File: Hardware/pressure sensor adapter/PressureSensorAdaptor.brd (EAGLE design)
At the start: 34.3 x 26.7 mm, 13 parts, among them IC1 RCV420P

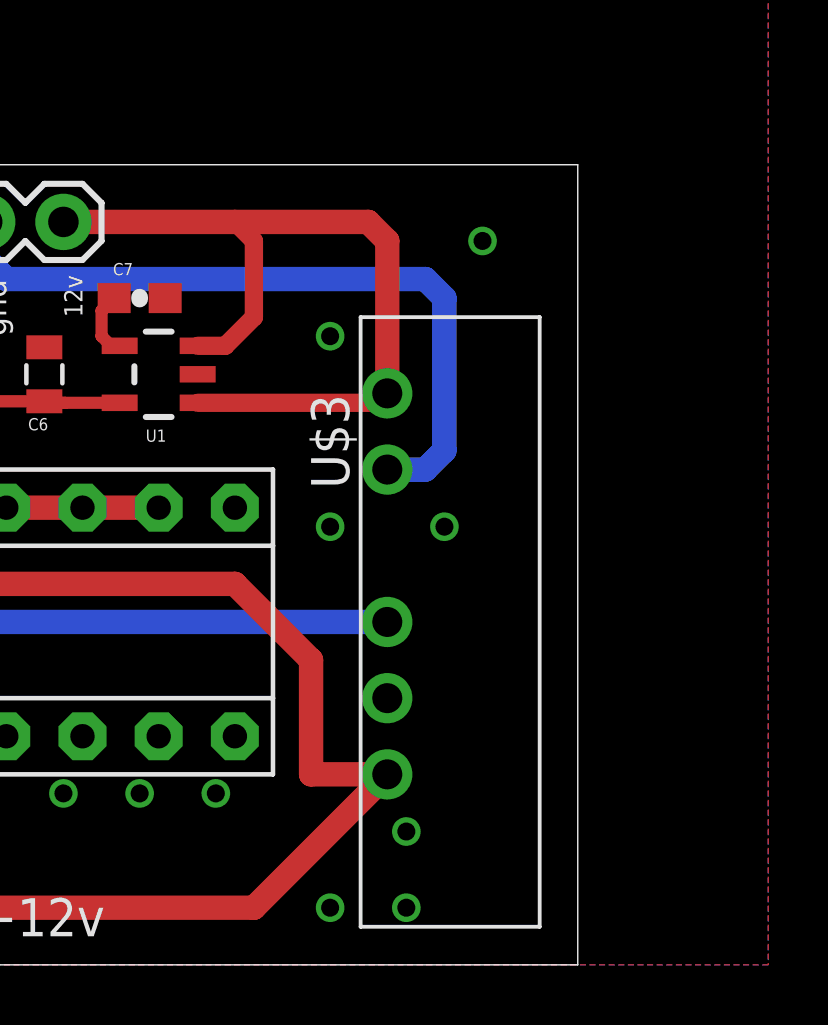
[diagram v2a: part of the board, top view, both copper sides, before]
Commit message: added bulk capacitance on 12v unisolated rail
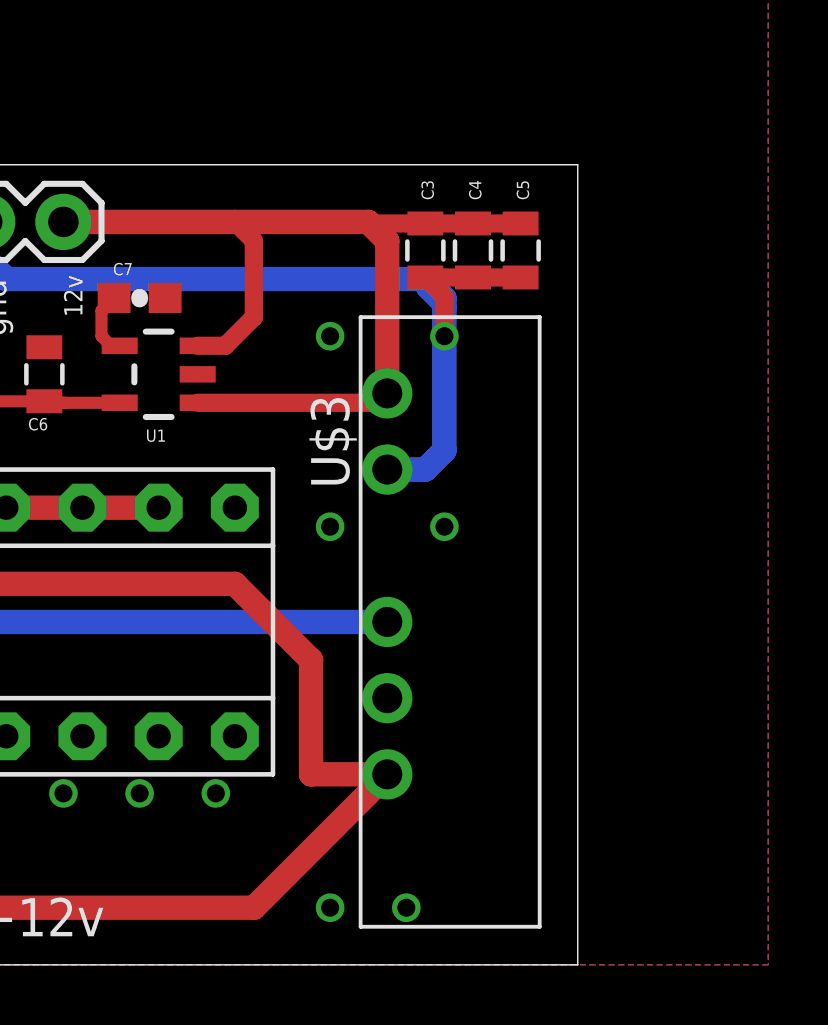
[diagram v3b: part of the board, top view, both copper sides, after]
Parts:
- added C3: 10uF, SparkFun-Capacitors:0805
- added C4: 0.1uf, SparkFun-Capacitors:0805
- added C5: 100pF, SparkFun-Capacitors:0805
- C8: value (none) -> 0.1uf
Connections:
- net 12V: now also C3.1, C4.1, C5.1
- net GND: now also C3.2, C4.2, C5.2
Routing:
- net GND: track 24.3 -> 30.9 mm, vias 0 -> 1
- net 12V: track 28.3 -> 33.4 mm
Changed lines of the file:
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@@
 <attribute name="NAME" x="18.796" y="22.987" size="0.4064" layer="25" font="vector"/>
 </element>
-<element name="C8" library="SparkFun-Capacitors" package="0805" value="" x="3.175" y="19.05" rot="R180"/>
+<element name="C8" library="SparkFun-Capacitors" package="0805" value="0.1uf" x="3.175" y="19.05" rot="R180"/>
 <element name="JP3" library="SparkFun-Connectors" package="1X05" value="" x="6.985" y="24.765" smashed="yes">
 <attribute name="VALUE" x="5.715" y="21.59" size="1.27" layer="27"/>
@@
 </element>
 <element name="U$1" library="RitLaunchInitiative" package="RITLAUNCH_LOGO_SMALLB" value="" x="20.32" y="13.97"/>
+<element name="C3" library="SparkFun-Capacitors" package="0805" value="10uF" x="29.21" y="23.8125" smashed="yes" rot="R270">
+<attribute name="DIGIKEY" value="490-3886-1-ND" x="29.21" y="23.8125" size="1.778" layer="27" rot="R270" display="off"/>
+<attribute name="NAME" x="29.083" y="26.162" size="0.4064" layer="25" rot="R270"/>
+</element>
+<element name="C4" library="SparkFun-Capacitors" package="0805" value="0.1uf" x="30.7975" y="23.8125" smashed="yes" rot="R270">
+<attribute name="NAME" x="30.6705" y="26.162" size="0.4064" layer="25" rot="R270"/>
+</element>
+<element name="C5" library="SparkFun-Capacitors" package="0805" value="100pF" x="32.385" y="23.8125" smashed="yes" rot="R270">
+<attribute name="NAME" x="32.258" y="26.162" size="0.4064" layer="25" rot="R270"/>
+</element>
 </elements>
 <signals>
@@
 <wire x1="27.94" y1="16.51" x2="29.21" y2="16.51" width="0.8128" layer="16"/>
 <wire x1="29.21" y1="16.51" x2="29.845" y2="17.145" width="0.8128" layer="16"/>
-<wire x1="29.845" y1="17.145" x2="29.845" y2="22.225" width="0.8128" layer="16"/>
+<wire x1="29.845" y1="17.145" x2="29.845" y2="20.955" width="0.8128" layer="16"/>
+<wire x1="29.845" y1="20.955" x2="29.845" y2="21.9075" width="0.8128" layer="16"/>
+<wire x1="29.845" y1="21.9075" x2="29.845" y2="22.225" width="0.8128" layer="16"/>
 <wire x1="29.845" y1="22.225" x2="29.21" y2="22.86" width="0.8128" layer="16"/>
 <wire x1="29.21" y1="22.86" x2="15.24" y2="22.86" width="0.8128" layer="16"/>
+<contactref element="C5" pad="2"/>
+<contactref element="C4" pad="2"/>
+<contactref element="C3" pad="2"/>
+<wire x1="32.385" y1="22.9125" x2="30.7975" y2="22.9125" width="0.6096" layer="1"/>
+<wire x1="30.7975" y1="22.9125" x2="29.21" y2="22.9125" width="0.6096" layer="1"/>
+<wire x1="29.21" y1="22.86" x2="29.21" y2="22.5425" width="0.6096" layer="16"/>
+<wire x1="29.21" y1="22.5425" x2="29.845" y2="21.9075" width="0.6096" layer="16"/>
+<via x="29.845" y="20.955" extent="1-16" drill="0.6" shape="octagon"/>
+<wire x1="29.845" y1="20.955" x2="29.845" y2="22.2775" width="0.6096" layer="1"/>
+<wire x1="29.845" y1="22.2775" x2="29.21" y2="22.9125" width="0.6096" layer="1"/>
 </signal>
 <signal name="VOUT">
@@
 <via x="1.905" y="23.495" extent="1-16" drill="0.6" shape="octagon" alwaysstop="yes"/>
 <via x="1.905" y="20.955" extent="1-16" drill="0.6" shape="octagon" alwaysstop="yes"/>
-<via x="28.575" y="4.445" extent="1-16" drill="0.6" shape="octagon"/>
 <via x="28.575" y="1.905" extent="1-16" drill="0.6" shape="octagon"/>
 <via x="26.035" y="14.605" extent="1-16" drill="0.6" shape="octagon"/>
-<via x="31.115" y="24.13" extent="1-16" drill="0.6" shape="octagon"/>
 <via x="13.335" y="20.955" extent="1-16" drill="0.6" shape="octagon"/>
 <via x="1.905" y="10.795" extent="1-16" drill="0.6" shape="octagon"/>
@@
 <wire x1="23.495" y1="21.59" x2="23.495" y2="24.13" width="0.6096" layer="1"/>
 <wire x1="23.495" y1="24.13" x2="22.86" y2="24.765" width="0.6096" layer="1"/>
+<contactref element="C5" pad="1"/>
+<contactref element="C4" pad="1"/>
+<contactref element="C3" pad="1"/>
+<wire x1="29.21" y1="24.7125" x2="27.3575" y2="24.7125" width="0.6096" layer="1"/>
+<wire x1="27.3575" y1="24.7125" x2="27.305" y2="24.765" width="0.6096" layer="1"/>
+<wire x1="29.21" y1="24.7125" x2="30.7975" y2="24.7125" width="0.6096" layer="1"/>
+<wire x1="30.7975" y1="24.7125" x2="32.385" y2="24.7125" width="0.6096" layer="1"/>
 </signal>
 <signal name="N$2">
